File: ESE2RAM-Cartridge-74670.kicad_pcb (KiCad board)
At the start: 2 copper layers, 100 x 60.5 mm, 27 parts, among them CN1 BUS_MSX, IC1 4M SRAM, IC2 4M SRAM, J1 8M, U1 74HC670, U2 74HC670, U3 74AHC138, U4 74AHC00, U5 74AHC32

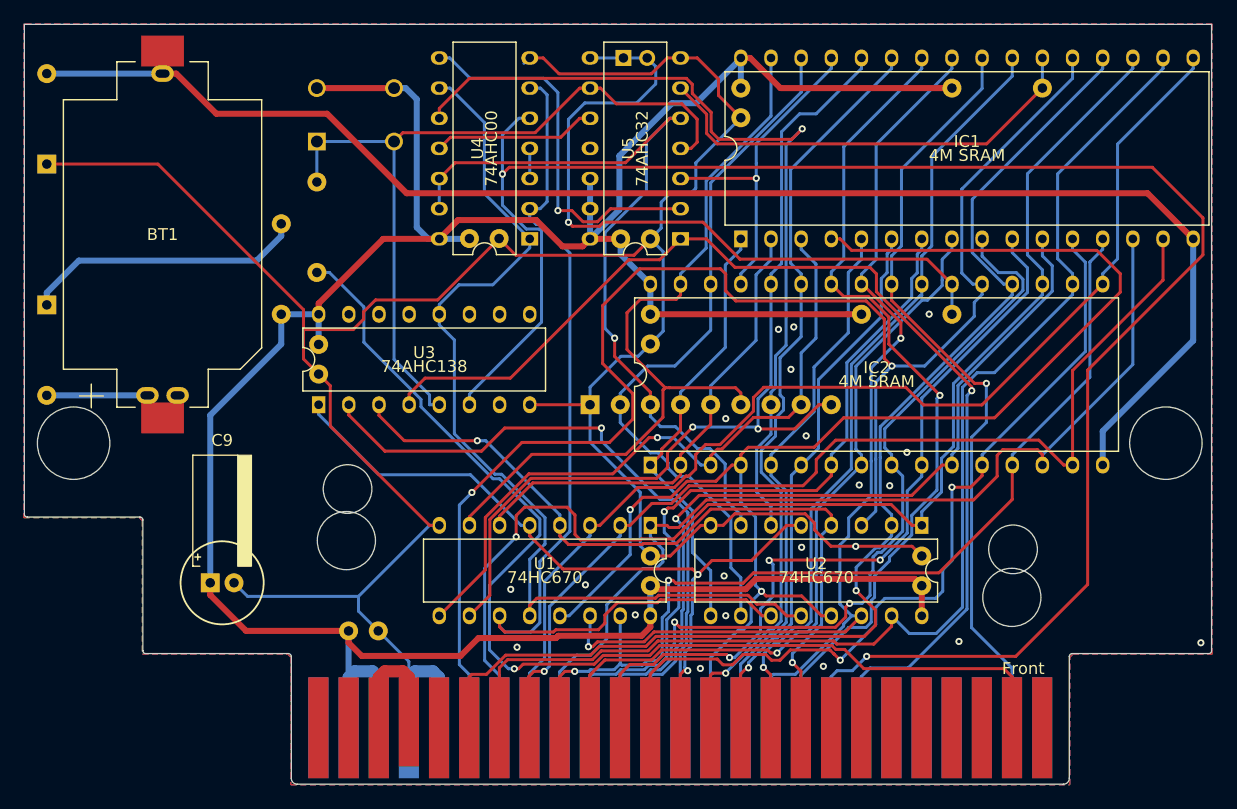
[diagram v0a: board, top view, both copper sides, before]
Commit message: Modified schematic data
一部のシンボルをプロジェクトのライブラリにコピーし、それに合わせ回路図を修正した
I copied some symbols into the project library and modified the schematic accordingly.
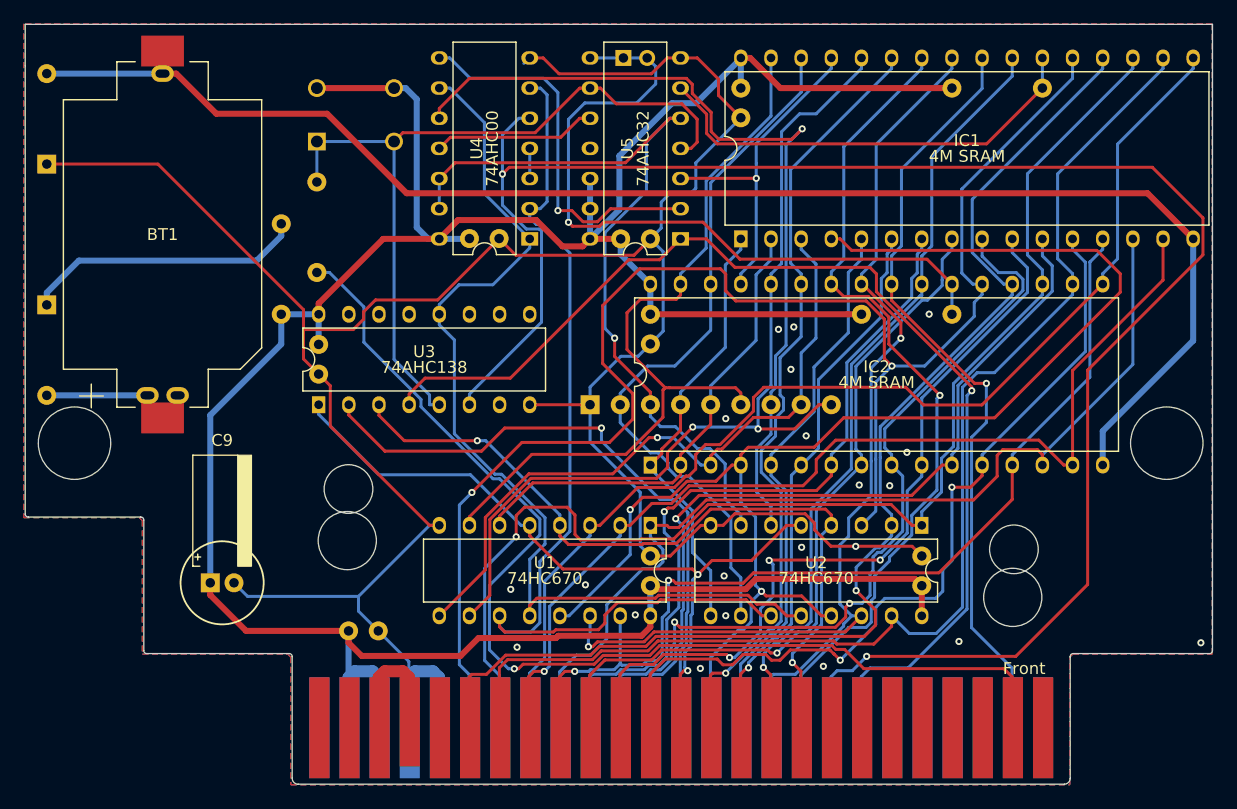
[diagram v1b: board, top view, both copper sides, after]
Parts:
- moved CN1 0.08 mm to (95.1, 159.1)
